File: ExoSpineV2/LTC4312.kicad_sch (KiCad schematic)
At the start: 14 parts, among them J18 JST PH 4pin, J28 JST PH 4pin, Q4 2N7002, U9 LTC4312IMS_PBF

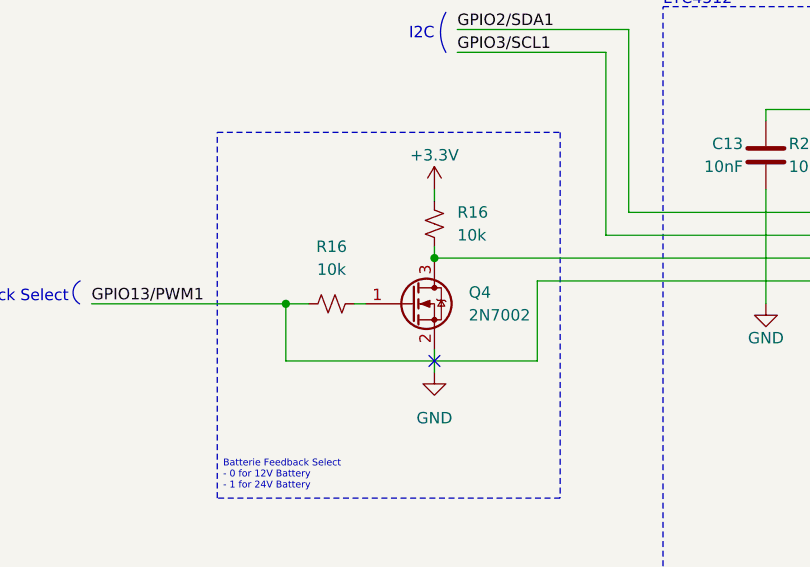
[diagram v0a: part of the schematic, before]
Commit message: changed symbols
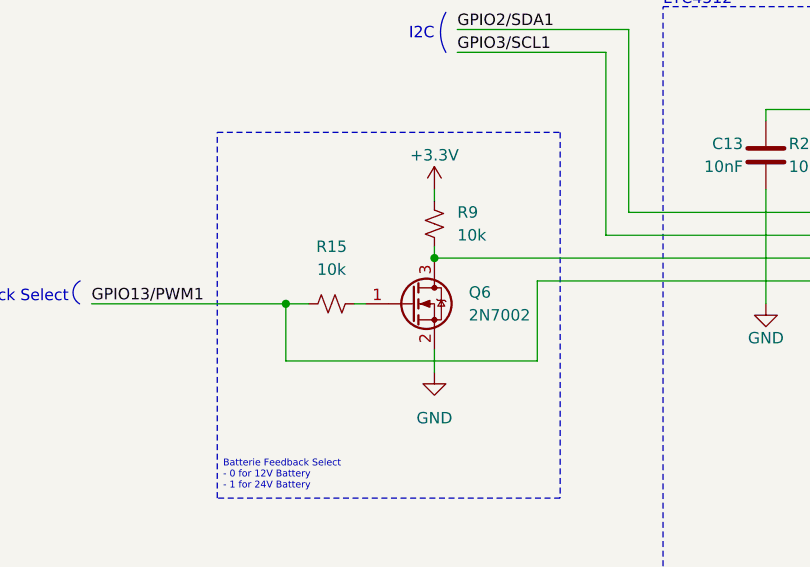
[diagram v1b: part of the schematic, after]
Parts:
- renumbered Q4 to Q6, R16 to R15, R16 to R9
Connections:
- no-connect marks 3 -> 2
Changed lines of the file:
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@@
   (no_connect (at 148.59 106.68))
   (no_connect (at 148.59 111.76))
-  (no_connect (at 95.25 99.06))
   (wire (pts (xy 172.72 72.39) (xy 172.72 71.12))
     (stroke (width 0) (type default))
@@
   (symbol (lib_id "Transistor_FET:2N7002") (at 92.71 92.71 0) (unit 1)
     (in_bom yes) (on_board yes) (dnp no) (fields_autoplaced)
-    (property "Reference" "Q4" (at 99.06 91.44 0)
+    (property "Reference" "Q6" (at 99.06 91.44 0)
       (effects (font (size 1.27 1.27)) (justify left))
     )
@@
     (instances
       (project "ExospineV2"
-        (path "/e63e39d7-6ac0-4ffd-8aa3-1841a4541b55"
-          (reference "Q4") (unit 1)
-        )
         (path "/e63e39d7-6ac0-4ffd-8aa3-1841a4541b55/20814431-03eb-459e-9e71-9431fed06066"
           (reference "Q6") (unit 1)
@@
   (symbol (lib_id "Device:R_Small_US") (at 95.25 83.82 0) (unit 1)
     (in_bom yes) (on_board yes) (dnp no) (fields_autoplaced)
-    (property "Reference" "R16" (at 97.79 82.55 0)
+    (property "Reference" "R9" (at 97.79 82.55 0)
       (effects (font (size 1.27 1.27)) (justify left))
     )
@@
     (instances
       (project "ExospineV2"
-        (path "/e63e39d7-6ac0-4ffd-8aa3-1841a4541b55/9042656c-fbb6-4ad3-be09-ad4e06445cda"
-          (reference "R16") (unit 1)
-        )
         (path "/e63e39d7-6ac0-4ffd-8aa3-1841a4541b55/20814431-03eb-459e-9e71-9431fed06066"
           (reference "R9") (unit 1)
@@
   (symbol (lib_id "Device:R_Small_US") (at 83.82 92.71 270) (unit 1)
     (in_bom yes) (on_board yes) (dnp no) (fields_autoplaced)
-    (property "Reference" "R16" (at 83.82 86.36 90)
+    (property "Reference" "R15" (at 83.82 86.36 90)
       (effects (font (size 1.27 1.27)))
     )
@@
     (instances
       (project "ExospineV2"
-        (path "/e63e39d7-6ac0-4ffd-8aa3-1841a4541b55/9042656c-fbb6-4ad3-be09-ad4e06445cda"
-          (reference "R16") (unit 1)
-        )
         (path "/e63e39d7-6ac0-4ffd-8aa3-1841a4541b55/20814431-03eb-459e-9e71-9431fed06066"
           (reference "R15") (unit 1)
